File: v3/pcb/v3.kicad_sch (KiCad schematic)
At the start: 412 parts, among them SW1 SW_Push, SW10 SW_Push, SW11 SW_Push, SW12 SW_Push, SW13 SW_Push, SW14 SW_Push, SW15 SW_Push, SW16 SW_Push, SW17 SW_Push, SW18 SW_Push, SW19 SW_Push, SW2 SW_Push, SW20 SW_Push, SW21 SW_Push, SW22 SW_Push, SW23 SW_Push, SW24 SW_Push, SW25 SW_Push, SW26 SW_Push, SW27 SW_Push, SW28 SW_Push, SW29 SW_Push, SW3 SW_Push, SW30 SW_Push, SW31 SW_Push, SW32 SW_Push, SW33 SW_Push, SW34 SW_Push, SW35 SW_Push, SW36 SW_Push, SW37 SW_Push, SW38 SW_Push, SW39 SW_Push, SW4 SW_Push, SW40 SW_Push, SW41 SW_Push, SW42 SW_Push, SW43 SW_Push, SW44 SW_Push, SW45 SW_Push, SW46 SW_Push, SW47 SW_Push, SW48 SW_Push, SW49 SW_Push, SW5 SW_Push, SW50 SW_Push, SW51 SW_Push, SW52 SW_Push, SW53 SW_Push, SW54 SW_Push, SW55 SW_Push, SW56 SW_Push, SW57 SW_Push, SW58 SW_Push, SW59 SW_Push, SW6 SW_Push, SW60 SW_Push, SW61 SW_Push, SW62 SW_Push, SW63 SW_Push, SW64 SW_Push, SW65 SW_Push, SW66 SW_Push, SW67 SW_Push, SW68 SW_Push, SW69 SW_Push, SW7 SW_Push, SW70 SW_Push, SW71 SW_Push, SW72 SW_Push, SW73 SW_Push, SW74 SW_Push, SW75 SW_Push, SW76 SW_Push, SW77 SW_Push, SW78 SW_Push, SW79 SW_Push, SW8 SW_Push, SW80 SW_Push, SW81 SW_Push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

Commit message: Finished USB and add pinouts for teensy
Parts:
- removed FB?: fb_0402_26ohm, Bonsai_C4:R_0402_1005Metric, symbol Bonsai_C4:fb_0402_26ohm
- added F1: 3A, prettylib:Fuse_1206_3216Metric, symbol Device:Polyfuse_Small
- added FB1: FerriteBead, Resistor_SMD:R_0402_1005Metric, symbol Device:FerriteBead
- added J2: Conn_01x21, Connector_PinHeader_2.00mm:PinHeader_1x21_P2.00mm_Vertical, symbol Connector_Generic:Conn_01x21
- added Q1: AO3401A, prettylib:SOT-23, symbol Transistor_FET:AO3401A
- added TP5: D+, TestPoint:TestPoint_THTPad_D1.5mm_Drill0.7mm, symbol Connector:TestPoint
- added TP6: D-, TestPoint:TestPoint_THTPad_D1.5mm_Drill0.7mm, symbol Connector:TestPoint
- added TP7: USB_VBUS, TestPoint:TestPoint_THTPad_D1.5mm_Drill0.7mm, symbol Connector:TestPoint
- added U3: LMV321, prettylib:SOT-23-5, symbol Amplifier_Operational:LMV321
- added U4: SRV0504, prettylib:SOT-23-6, symbol YAEMK:SRV0504
- gave numbers to parts that had none: 3
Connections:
- net VUSB is gone; now on net +5V: U1.54 (VUSB), U2.1 (VCCA)
- net 3V3REF: now also TP2.1
- net GND: now also U1.27 (GND), U1.61 (GND), U1.62 (GND), FB1.2, J2.21 (Pin_21), U4.2 (GND)
- net USB_D+: now also TP5.1, U4.3 (I/O2)
- net USB_D-: now also TP6.1, U4.1 (I/O1)
- net +5V: now reaches RGB69.1 (VDD), RGB70.1 (VDD), RGB71.1 (VDD), RGB72.1 (VDD), RGB73.1 (VDD), RGB74.1 (VDD), RGB75.1 (VDD), RGB76.1 (VDD), RGB77.1 (VDD), RGB78.1 (VDD), RGB79.1 (VDD), RGB80.1 (VDD), RGB81.1 (VDD), RGB82.1 (VDD), RGB83.1 (VDD), RGB84.1 (VDD), RGB85.1 (VDD), RGB86.1 (VDD)
- net +5V: now also C1.1, C10.1, C11.1, C12.1, C13.1, C14.1, C15.1, C16.1, C17.1, C18.1, C19.1, C2.1, C20.1, C21.1, C22.1, C23.1, C24.1, C25.1, C26.1, C27.1, C28.1, C29.1, C3.1, C30.1, C31.1, C32.1, C33.1, C34.1, C35.1, C36.1, C37.1, C38.1, C39.1, C4.1, C40.1, C41.1, C42.1, C43.1, C44.1, C45.1, C46.1, C47.1, C48.1, C49.1, C5.1, C50.1, C51.1, C52.1, C53.1, C54.1, C55.1, C56.1, C57.1, C58.1, C59.1, C6.1, C60.1, C61.1, C62.1, C63.1, C64.1, C65.1, C66.1, C67.1, C68.1, C69.1, C7.1, C70.1, C71.1, C72.1, C73.1, C74.1, C75.1, C76.1, C77.1, C78.1, C79.1, C8.1, C80.1, C81.1, C82.1, C83.1, C84.1, C85.1, C86.1, C87.1, C88.1, C89.1, C9.1, C90.1, C91.1, C92.1, C93.1, C94.1, C95.1, C96.1, C97.1, C98.1, C99.1, RGB1.1 (VDD), RGB10.1 (VDD), RGB11.1 (VDD), RGB12.1 (VDD), RGB13.1 (VDD), RGB14.1 (VDD), RGB15.1 (VDD), RGB16.1 (VDD), RGB17.1 (VDD), RGB18.1 (VDD), RGB19.1 (VDD), RGB2.1 (VDD), RGB20.1 (VDD), RGB21.1 (VDD), RGB22.1 (VDD), RGB23.1 (VDD), RGB24.1 (VDD), RGB25.1 (VDD), RGB26.1 (VDD), RGB27.1 (VDD), RGB28.1 (VDD), RGB29.1 (VDD), RGB3.1 (VDD), RGB30.1 (VDD), RGB31.1 (VDD), RGB32.1 (VDD), RGB33.1 (VDD), RGB34.1 (VDD), RGB35.1 (VDD), RGB36.1 (VDD), RGB37.1 (VDD), RGB38.1 (VDD), RGB39.1 (VDD), RGB4.1 (VDD), RGB40.1 (VDD), RGB41.1 (VDD), RGB42.1 (VDD), RGB43.1 (VDD), RGB44.1 (VDD), RGB45.1 (VDD), RGB46.1 (VDD), RGB47.1 (VDD), RGB48.1 (VDD), RGB49.1 (VDD), RGB5.1 (VDD), RGB50.1 (VDD), RGB51.1 (VDD), RGB52.1 (VDD), RGB53.1 (VDD), RGB54.1 (VDD), RGB55.1 (VDD), RGB56.1 (VDD), RGB57.1 (VDD), RGB58.1 (VDD), RGB59.1 (VDD), RGB6.1 (VDD), RGB60.1 (VDD), RGB61.1 (VDD), RGB62.1 (VDD), RGB63.1 (VDD), RGB64.1 (VDD), RGB65.1 (VDD), RGB66.1 (VDD), RGB67.1 (VDD), RGB68.1 (VDD), RGB7.1 (VDD), RGB8.1 (VDD), RGB87.1 (VDD), RGB88.1 (VDD), RGB89.1 (VDD), RGB9.1 (VDD), RGB90.1 (VDD), RGB91.1 (VDD), RGB92.1 (VDD), RGB93.1 (VDD), RGB94.1 (VDD), RGB95.1 (VDD), RGB96.1 (VDD), RGB97.1 (VDD), RGB98.1 (VDD), RGB99.1 (VDD), J2.1 (Pin_1), Q1.2 (S), U3.1 (+), U3.5 (V+)
- net VBAT: now reaches U1.25 (VBat)
- net VBAT: now also J2.19 (Pin_19)
- net 3.3V: now reaches U1.26 (3.3V)
- net 3.3V: now also J2.16 (Pin_16)
- net PROGRAM: now reaches U1.28 (Program)
- net PROGRAM: now also J2.17 (Pin_17)
- net RESET: now reaches U1.29 (Reset)
- net RESET: now also J2.18 (Pin_18)
- net A21_DAC0: now reaches U1.37 (A21_DAC0)
- net A21_DAC0: now also J2.14 (Pin_14)
- net A22_DAC1: now reaches U1.38 (A22_DAC1)
- net A22_DAC1: now also J2.15 (Pin_15)
- net PIN_13_LED: now reaches U1.40 (13_SCK0_LED)
- net PIN_13_LED: now also J2.2 (Pin_2)
- net PIN_14_A0_SCK0: now reaches U1.41 (14_A0_PWM_SCK0)
- net PIN_14_A0_SCK0: now also J2.3 (Pin_3)
- net PIN_15_A1_CS0: now reaches U1.42 (15_A1_CS0_Touch)
- net PIN_15_A1_CS0: now also J2.4 (Pin_4)
- net PIN_16_A2_SCL0: now reaches U1.43 (16_A2_SCL0_Touch)
- net PIN_16_A2_SCL0: now also J2.5 (Pin_5)
- net PIN_17_A3_SDA0: now reaches U1.44 (17_A3_SDA0_Touch)
- net PIN_17_A3_SDA0: now also J2.6 (Pin_6)
- net PIN18_A4_SDA0: now reaches U1.45 (18_A4_SDA0_Touch)
- net PIN18_A4_SDA0: now also J2.7 (Pin_7)
- net PIN_19_A5_SCL0: now reaches U1.46 (19_A5_SCL0_Touch)
- net PIN_19_A5_SCL0: now also J2.8 (Pin_8)
- net PIN_20_A6: now reaches U1.47 (20_A6_PWM_CS0_SCK1)
- net PIN_20_A6: now also J2.9 (Pin_9)
- net PIN_21_A7: now reaches U1.48 (21_A7_PWM_CS0_MOSI1)
- net PIN_21_A7: now also J2.10 (Pin_10)
- net PIN_22_A8: now reaches U1.49 (22_A8_PWM_Touch)
- net PIN_22_A8: now also J2.11 (Pin_11)
- net PIN_23_A9: now reaches U1.50 (23_A9_PWM_Touch)
- net PIN_23_A9: now also J2.12 (Pin_12)
- net AGND: now reaches U1.52 (AGND)
- net AGND: now also J2.20 (Pin_20)
- net AREF: now reaches U1.55 (AREF)
- net AREF: now also J2.13 (Pin_13)
- net at J1.S1 (SHIELD): now also FB1.1
- net USB_VBUS: now reaches J1.A4 (VBUS), J1.A9 (VBUS), J1.B4 (VBUS), J1.B9 (VBUS)
- net USB_VBUS: now also F1.2, TP7.1, U4.5 (VBUS)
- removed net RGB_VDD: C1.1, C10.1, C11.1, C12.1, C13.1, C14.1, C15.1, C16.1, C17.1, C18.1, C19.1, C2.1, C20.1, C21.1, C22.1, C23.1, C24.1, C25.1, C26.1, C27.1, C28.1, C29.1, C3.1, C30.1, C31.1, C32.1, C33.1, C34.1, C35.1, C36.1, C37.1, C38.1, C39.1, C4.1, C40.1, C41.1, C42.1, C43.1, C44.1, C45.1, C46.1, C47.1, C48.1, C49.1, C5.1, C50.1, C51.1, C52.1, C53.1, C54.1, C55.1, C56.1, C57.1, C58.1, C59.1, C6.1, C60.1, C61.1, C62.1, C63.1, C64.1, C65.1, C66.1, C67.1, C68.1, C69.1, C7.1, C70.1, C71.1, C72.1, C73.1, C74.1, C75.1, C76.1, C77.1, C78.1, C79.1, C8.1, C80.1, C81.1, C82.1, C83.1, C84.1, C85.1, C86.1, C87.1, C88.1, C89.1, C9.1, C90.1, C91.1, C92.1, C93.1, C94.1, C95.1, C96.1, C97.1, C98.1, C99.1, RGB1.1 (VDD), RGB10.1 (VDD), RGB11.1 (VDD), RGB12.1 (VDD), RGB13.1 (VDD), RGB14.1 (VDD), RGB15.1 (VDD), RGB16.1 (VDD), RGB17.1 (VDD), RGB18.1 (VDD), RGB19.1 (VDD), RGB2.1 (VDD), RGB20.1 (VDD), RGB21.1 (VDD), RGB22.1 (VDD), RGB23.1 (VDD), RGB24.1 (VDD), RGB25.1 (VDD), RGB26.1 (VDD), RGB27.1 (VDD), RGB28.1 (VDD), RGB29.1 (VDD), RGB3.1 (VDD), RGB30.1 (VDD), RGB31.1 (VDD), RGB32.1 (VDD), RGB33.1 (VDD), RGB34.1 (VDD), RGB35.1 (VDD), RGB36.1 (VDD), RGB37.1 (VDD), RGB38.1 (VDD), RGB39.1 (VDD), RGB4.1 (VDD), RGB40.1 (VDD), RGB41.1 (VDD), RGB42.1 (VDD), RGB43.1 (VDD), RGB44.1 (VDD), RGB45.1 (VDD), RGB46.1 (VDD), RGB47.1 (VDD), RGB48.1 (VDD), RGB49.1 (VDD), RGB5.1 (VDD), RGB50.1 (VDD), RGB51.1 (VDD), RGB52.1 (VDD), RGB53.1 (VDD), RGB54.1 (VDD), RGB55.1 (VDD), RGB56.1 (VDD), RGB57.1 (VDD), RGB58.1 (VDD), RGB59.1 (VDD), RGB6.1 (VDD), RGB60.1 (VDD), RGB61.1 (VDD), RGB62.1 (VDD), RGB63.1 (VDD), RGB64.1 (VDD), RGB65.1 (VDD), RGB66.1 (VDD), RGB67.1 (VDD), RGB68.1 (VDD), RGB7.1 (VDD), RGB8.1 (VDD), RGB87.1 (VDD), RGB88.1 (VDD), RGB89.1 (VDD), RGB9.1 (VDD), RGB90.1 (VDD), RGB91.1 (VDD), RGB92.1 (VDD), RGB93.1 (VDD), RGB94.1 (VDD), RGB95.1 (VDD), RGB96.1 (VDD), RGB97.1 (VDD), RGB98.1 (VDD), RGB99.1 (VDD), TP2.1
- new net: F1.1, Q1.3 (D), U3.3 (-)
- new net: Q1.1 (G), U3.4
- new net VSS: U3.2 (V-)
- no-connect marks 8 -> 40
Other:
- moved on the sheet: H1, H2, H3, H4, H5, H6

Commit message: Add logo LEDS, adjust zones, remove unnecessary components
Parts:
- removed F1: 3A, prettylib:Fuse_1206_3216Metric, symbol Device:Polyfuse_Small
- removed Q1: AO3401A, prettylib:SOT-23, symbol Transistor_FET:AO3401A
- removed TP7: USB_VBUS, TestPoint:TestPoint_THTPad_D1.5mm_Drill0.7mm, symbol Connector:TestPoint
- removed U3: LMV321, prettylib:SOT-23-5, symbol Amplifier_Operational:LMV321
- removed U4: SRV0504, prettylib:SOT-23-6, symbol YAEMK:SRV0504
- added RGB_LOGO1, RGB_LOGO2, RGB_LOGO3, RGB_LOGO4: SK6812Mini-e, prettylib:SK6812_mini_e_flipable, symbol YAEMK:SK6812MINI-E
- added TP3: 5V, TestPoint:TestPoint_THTPad_D1.5mm_Drill0.7mm, symbol Connector:TestPoint
- added TP4: GND, TestPoint:TestPoint_THTPad_D1.5mm_Drill0.7mm, symbol Connector:TestPoint
- renumbered TP5 to TP1, TP6 to TP2, TP1 to TP5, TP2 to TP6, TP3 to TP7, TP4 to TP8
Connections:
- net USB_VBUS is gone; now on net +5V: J1.A4 (VBUS), J1.A9 (VBUS), J1.B4 (VBUS), J1.B9 (VBUS)
- net +5V: now also RGB_LOGO1.1 (VDD), RGB_LOGO2.1 (VDD), RGB_LOGO3.1 (VDD), RGB_LOGO4.1 (VDD), TP3.1
- net GND: now also RGB_LOGO1.3 (VSS), RGB_LOGO2.3 (VSS), RGB_LOGO3.3 (VSS), RGB_LOGO4.3 (VSS), TP4.1
- net RGB_DATA: now also RGB_LOGO1.4 (DIN), RGB_LOGO2.4 (DIN), RGB_LOGO3.4 (DIN), RGB_LOGO4.4 (DIN); no longer RGB13.4 (DIN)
- new net: RGB13.4 (DIN), RGB_LOGO1.2 (DOUT), RGB_LOGO2.2 (DOUT), RGB_LOGO3.2 (DOUT), RGB_LOGO4.2 (DOUT)
- no-connect marks 40 -> 38
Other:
- moved on the sheet: U2

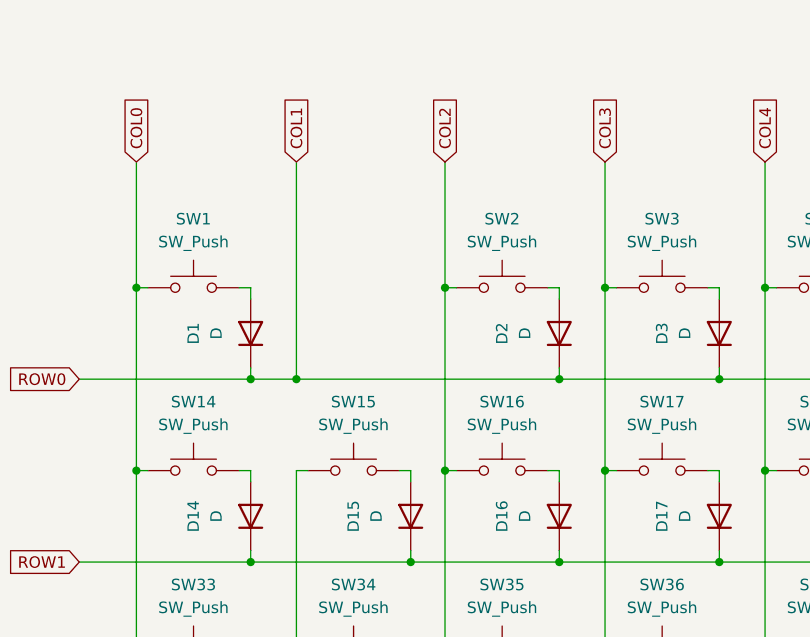
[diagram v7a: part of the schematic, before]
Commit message: Add column tracks
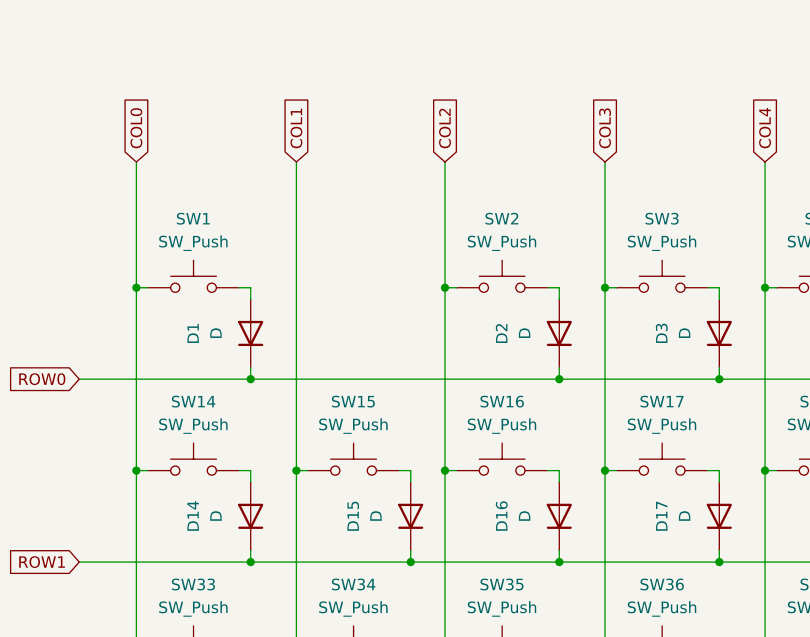
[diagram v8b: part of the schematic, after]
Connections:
- net COL1: now also SW15.1, SW34.1, SW53.1, SW88.1; no longer D1.1 (K), D10.1 (K), D11.1 (K), D12.1 (K), D13.1 (K), D2.1 (K), D3.1 (K), D4.1 (K), D5.1 (K), D6.1 (K), D7.1 (K), D8.1 (K), D9.1 (K), U1.7 (5_PWM_TX1_MISO1)
- new net ROW0: D1.1 (K), D10.1 (K), D11.1 (K), D12.1 (K), D13.1 (K), D2.1 (K), D3.1 (K), D4.1 (K), D5.1 (K), D6.1 (K), D7.1 (K), D8.1 (K), D9.1 (K), U1.7 (5_PWM_TX1_MISO1)
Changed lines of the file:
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@@
   (junction (at 514.35 309.88) (diameter 0) (color 0 0 0 0)
   )
-  (junction (at 57.15 77.47) (diameter 0) (color 0 0 0 0)
-  )
   (junction (at 203.2 429.26) (diameter 0) (color 0 0 0 0)
   )
@@
   (junction (at 157.48 138.43) (diameter 0) (color 0 0 0 0)
   )
+  (junction (at 57.15 87.63) (diameter 0) (color 0 0 0 0)
+  )
   (junction (at 218.44 220.98) (diameter 0) (color 0 0 0 0)
   )
@@
     (stroke (width 0) (type default) (color 0 0 0 0))
   )
-  (wire (pts (xy 57.15 77.47) (xy 86.36 77.47))
+  (wire (pts (xy 52.07 77.47) (xy 86.36 77.47))
     (stroke (width 0) (type default) (color 0 0 0 0))
   )
@@
     (stroke (width 0) (type default) (color 0 0 0 0))
   )
-  (wire (pts (xy 52.07 77.47) (xy 57.15 77.47))
-    (stroke (width 0) (type default) (color 0 0 0 0))
-  )
   (wire (pts (xy 157.48 128.27) (xy 157.48 129.54))
     (stroke (width 0) (type default) (color 0 0 0 0))
@@
     (stroke (width 0) (type default) (color 0 0 0 0))
   )
-  (wire (pts (xy 57.15 53.34) (xy 57.15 77.47))
-    (stroke (width 0) (type default) (color 0 0 0 0))
-  )
   (wire (pts (xy 49.53 228.6) (xy 49.53 269.24))
     (stroke (width 0) (type default) (color 0 0 0 0))
@@
     (stroke (width 0) (type default) (color 0 0 0 0))
   )
+  (wire (pts (xy 57.15 53.34) (xy 57.15 87.63))
+    (stroke (width 0) (type default) (color 0 0 0 0))
+  )
